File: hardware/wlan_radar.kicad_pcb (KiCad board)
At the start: 4 copper layers, 55 x 25 mm, 126 parts, among them P1 CONN_2, P2 CONN_2, P3 CONN_2, P4 CONN_6, Q1 MOS_P_BSS84, U1 SST11LP12, U10 LTC6242, U11 LT6230, U12 MCP4017, U13 USB-MICRO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

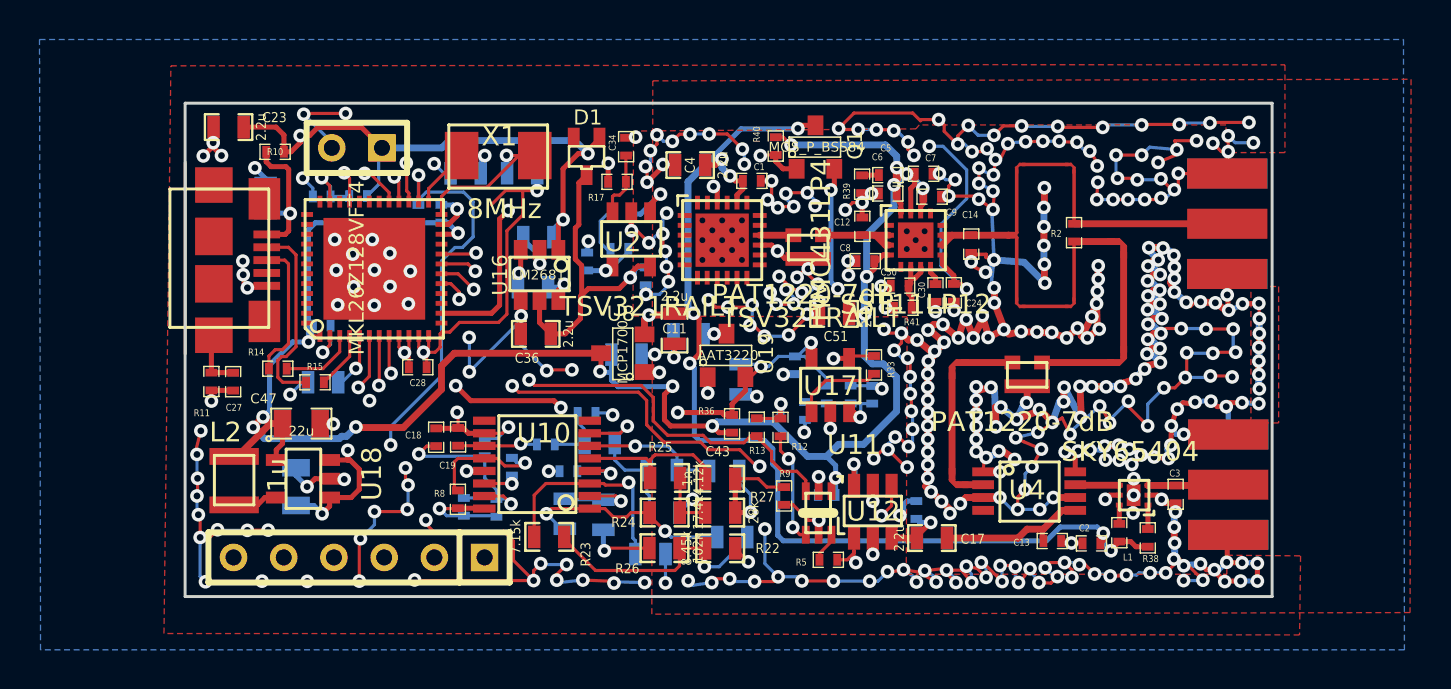
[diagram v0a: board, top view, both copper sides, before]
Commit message: Fix hardware mistakes
This commit adds fixes some of the mistakes identified after the
board was ordered.

Add 100n capacitor to MCUs reset pin to fix programming issues.

Add series connection of resistor and capacitor in parallel
with mixer output amplifier to fix the DC balance issue.

Remove the now unneeded capacitor and resistor
after the low-pass filter.

Add 200k resistor in feedback path of single-ended to differential
conversion circuit to solve the issue with limited input voltage range.
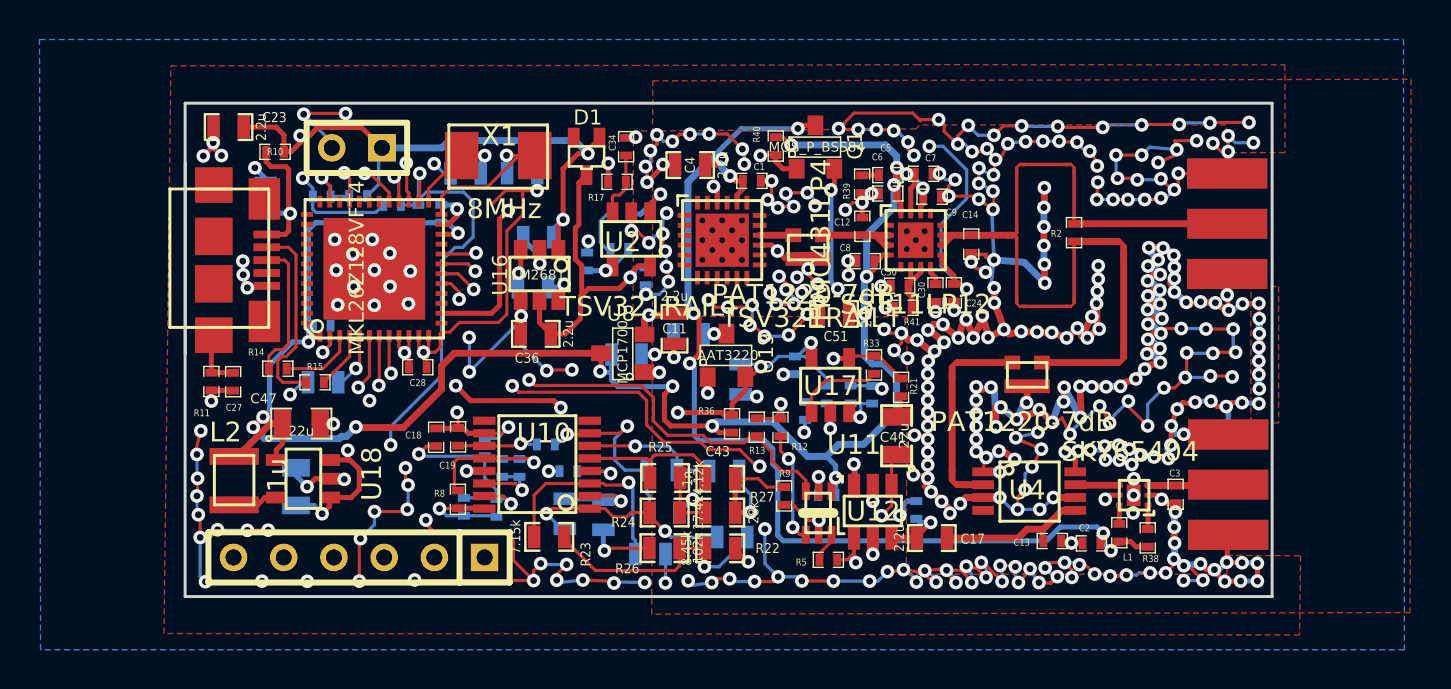
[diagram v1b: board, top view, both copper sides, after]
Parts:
- added C52: 100n, SMD_Packages:SMD-0402_c, B.Cu at (120.0, 87.8)
- added R42: 200k, SMD_Packages:SMD-0402_r, B.Cu at (125.6, 101.2)
- C41: value 2.2u -> 22u; footprint SMD_Packages:SMD-0603_c -> SMD_Packages:SMD-0805; moved to F.Cu
- R21: value 10k -> 50; moved to F.Cu
- R9: value 50 -> 1.5k
- moved R21 16.0 mm to (145.8, 97.1), turned to 90 degrees
- moved C41 15.0 mm to (145.5, 99.5), turned to 90 degrees
- moved C21 0.39 mm to (126.5, 101.2)
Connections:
- C41 pad 2: Net-(C40-Pad1) -> Net-(C41-Pad2)
- R21 pad 1: /VG -> Net-(C41-Pad2)
- R21 pad 2: Net-(C41-Pad1) -> /VG
- R7 pad 2: Net-(C41-Pad1) -> Net-(C40-Pad1)
- R9 pad 1: Net-(R9-Pad1) -> Net-(C41-Pad1)
- U11 pad 4: Net-(R9-Pad1) -> Net-(C41-Pad1)
- U12 pad 5: Net-(R9-Pad1) -> Net-(C41-Pad1)
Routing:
- net Net-(R9-Pad1): track 7.82 -> 0.00 mm, vias 2 -> 0
- net Net-(C41-Pad1): track 3.20 -> 9.51 mm, vias 0 -> 2
- net /VG: track 63.3 -> 57.1 mm, vias 8 -> 7
- net GND: track 523.7 -> 521.3 mm, vias 411 -> 404
- net Net-(C40-Pad1): track 8.08 -> 10.1 mm, vias 1 -> 2
- net Net-(C21-Pad1): track 6.24 -> 7.44 mm
- net Net-(C41-Pad2): track 0.00 -> 1.14 mm
- net /mcu/~RESET: track 26.3 -> 27.4 mm
